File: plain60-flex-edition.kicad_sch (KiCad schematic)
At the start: 173 parts, among them J1 HRO-TYPE-C-31-M-12, J2 ISP, J3 ai03_ud, K1 KEYSW, K10 KEYSW, K11 KEYSW, K12 KEYSW, K13 KEYSW, K14 KEYSW, K15 KEYSW, K15-1 KEYSW, K16 KEYSW, K17 KEYSW, K18 KEYSW, K19 KEYSW, K2 KEYSW, K20 KEYSW, K21 KEYSW, K22 KEYSW, K23 KEYSW, K24 KEYSW, K25 KEYSW, K26 KEYSW, K27 KEYSW, K28 KEYSW, K29 KEYSW, K3 KEYSW, K31 KEYSW, K31-1 KEYSW, K32 KEYSW, K33 KEYSW, K34 KEYSW, K35 KEYSW, K36 KEYSW, K37 KEYSW, K38 KEYSW, K39 KEYSW, K4 KEYSW, K40 KEYSW, K41 KEYSW, K42 KEYSW, K43 KEYSW, K44 KEYSW, K44-1 KEYSW, K46 KEYSW, K46-1 KEYSW, K47 KEYSW, K48 KEYSW, K49 KEYSW, K5 KEYSW, K50 KEYSW, K51 KEYSW, K52 KEYSW, K53 KEYSW, K54 KEYSW, K55 KEYSW, K56 KEYSW, K57 KEYSW, K58 KEYSW, K58-1 KEYSW, K59 KEYSW, K6 KEYSW, K61 KEYSW, K61-1 KEYSW, K62 KEYSW, K62-1 KEYSW, K63 KEYSW, K63-1 KEYSW, K67 KEYSW, K67-1 KEYSW, K7 KEYSW, K71 KEYSW, K72 KEYSW, K72-1 KEYSW, K73 KEYSW, K73-1 KEYSW, K74 KEYSW, K74-1 KEYSW, K8 KEYSW, K9 KEYSW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

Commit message: added first iteration of refactoring
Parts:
- removed C1: 1u, Keeb_components:C_0805, symbol Device:C
- removed C2, C3, C4, C5: 0.1u, Keeb_components:C_0805, symbol Device:C
- removed C6: 4.7u, Keeb_components:C_0805, symbol Device:C
- removed F1: Polyfuse, Keeb_components:R_0805, symbol Device:Polyfuse
- removed H1: B0, footprints:free_pin, symbol Connector_Generic:Conn_01x01
- removed J1: HRO-TYPE-C-31-M-12, Keeb_components:HRO-TYPE-C-31-M-12, symbol Type-C:HRO-TYPE-C-31-M-12
- removed J2: ISP, Keeb_components:isp_standard, symbol Connector_Generic:Conn_02x03_Odd_Even
- removed J3: ai03_ud, Keeb_components:JST_SH_SM04B-SRSS-TB_1x04-1MP_P1.00mm_Horizontal, symbol Connector_Generic:Conn_01x04
- removed LS1: Speaker, Keeb_components:speaker_AST1109MLTRQ, symbol Device:Speaker
- removed R1, R2: 22, Keeb_components:R_0805, symbol Device:R
- removed R3, R4: 5.1k, Keeb_components:R_0805, symbol Device:R
- removed R5, R6: 10k, Keeb_components:R_0805, symbol Device:R
- removed SW1: SW_PUSH, Button_Switch_SMD:SW_SPST_TL3342, symbol keyboard_parts:SW_PUSH
- removed U1: ATmega32U4, Keeb_components:ATMEGA32U4, symbol atmel:ATmega32U4
- removed U2: USBLC6-2SC6, Keeb_components:USBLC6-2SC6, symbol keyboard_parts:USBLC6-2SC6
- removed X1: XTAL_GND, Keeb_components:Resonator_SMD_muRata_CSTNExxV-3Pin-p1.2, symbol keyboard_parts:XTAL_GND
- added J1: 4P4C, Connector_JST:JST_PH_S4B-PH-K_1x04_P2.00mm_Horizontal, symbol Connector:4P4C
- added U1: ProS3, footprints2:ProS3_TH, symbol ProS3:ProS3
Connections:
- net GND: now also J1.1, U1.2 (GND)
- net col0: now also U1.31 (IO34)
- net col1: now also U1.28 (IO7)
- net col10: now also U1.13 (IO16)
- net col11: now also U1.14 (IO15)
- net col12: now also U1.15 (IO14)
- net col13: now also U1.16 (IO13)
- net col14: now also U1.17 (IO12)
- net col2: now also U1.19 (IO41)
- net col3: now also U1.18 (IO42)
- net col4: now also U1.6 (IO2)
- net col5: now also U1.7 (IO3)
- net col6: now also U1.8 (IO4)
- net col7: now also U1.9 (IO5)
- net col8: now also U1.10 (IO21)
- net col9: now also U1.12 (LDO2_OUT)
- net row0: now also U1.34 (IO35)
- net row1: now also U1.33 (IO37)
- net row2: now also U1.32 (IO36)
- net row3: now also U1.22 (IO38)
- net row4: now also U1.21 (IO39)
- new net 5V: J1.2, U1.3 (5V)
- new net display SCL: J1.4, U1.30 (IO9)
- new net display SDA: J1.3, U1.29 (IO8)
- new net pin00 removed: U1.11 (IO0)
- new net pin03 unused: U1.27 (IO6)
- new net rgb R1: U1.20 (IO40)
- new net rx: U1.23 (RX)
- new net tx: U1.24 (TX)
- no-connect marks 12 -> 9
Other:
- moved on the sheet: D1, D10, D11, D12, D13, D14, D15, D16, D17, D18, D19, D2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

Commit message: tuning
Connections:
- net tx is gone; now on net pin00 removed: U1.24 (TX)
- net col0: now also U1.5 (IO1); no longer U1.31 (IO34)
- net pin00 removed: no longer U1.11 (IO0)
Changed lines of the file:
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@@
     )
   )
-  (global_label "col0" (shape input) (at 51.308 35.814 180)
-    (effects (font (size 0.9906 0.9906)) (justify right))
-    (property "Intersheet References" "${INTERSHEET_REFS}" (id 0) (at 245.618 96.774 0)
+  (global_label "col0" (shape input) (at 79.248 38.608 0)
+    (effects (font (size 0.9906 0.9906)) (justify left))
+    (property "Intersheet References" "${INTERSHEET_REFS}" (id 0) (at -115.062 -22.352 0)
       (effects (font (size 1.27 1.27)) hide)
     )
@@
     (property "Intersheet References" "${INTERSHEET_REFS}" (id 0) (at 16.764 -36.576 0)
       (effects (font (size 1.27 1.27)) hide)
-    )
-  )
-  (global_label "tx" (shape input) (at 51.308 53.848 180)
-    (effects (font (size 0.9906 0.9906)) (justify right))
-    (property "Intersheet References" "${INTERSHEET_REFS}" (id 0) (at 245.618 117.348 0)
-      (effects (font (size 0.9906 0.9906)) hide)
     )
   )
@@
     )
   )
-  (global_label "pin00 removed" (shape input) (at 79.248 53.848 0)
-    (effects (font (size 0.9906 0.9906)) (justify left))
-    (property "Intersheet References" "${INTERSHEET_REFS}" (id 0) (at -115.062 -7.112 0)
+  (global_label "pin00 removed" (shape input) (at 51.308 53.848 180)
+    (effects (font (size 0.9906 0.9906)) (justify right))
+    (property "Intersheet References" "${INTERSHEET_REFS}" (id 0) (at 245.618 114.808 0)
       (effects (font (size 0.9906 0.9906)) hide)
     )

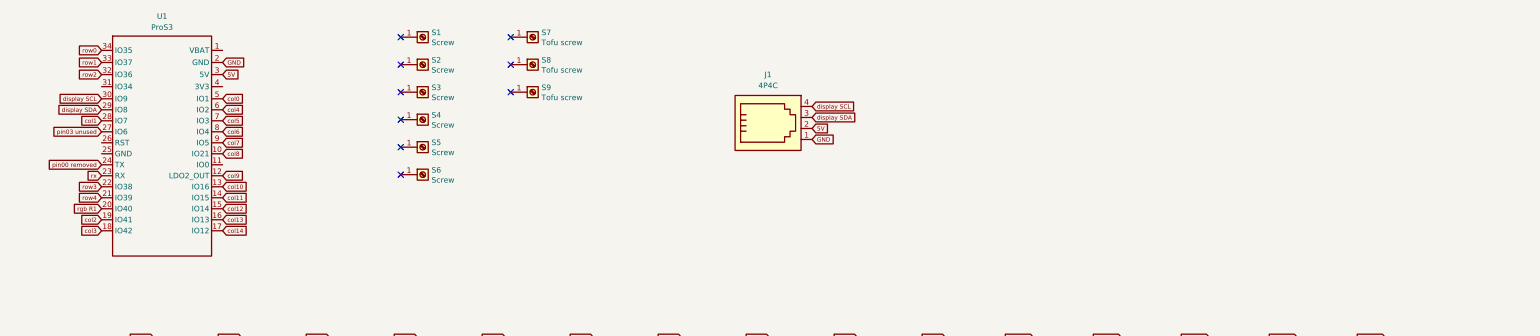
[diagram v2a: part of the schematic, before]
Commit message: added underglow leds
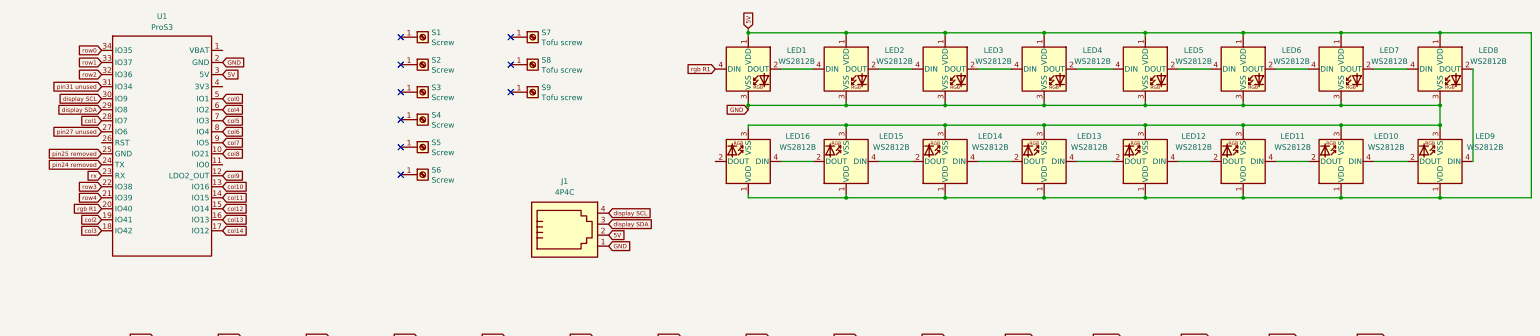
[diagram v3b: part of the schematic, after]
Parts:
- added LED1, LED10, LED11, LED12, LED13, LED14, LED15, LED16, LED2, LED3, LED4, LED5, LED6, LED7, LED8, LED9: WS2812B, LED_SMD:LED_WS2812B_PLCC4_5.0x5.0mm_P3.2mm, symbol LED:WS2812B
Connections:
- net 5V: now also LED1.1 (VDD), LED10.1 (VDD), LED11.1 (VDD), LED12.1 (VDD), LED13.1 (VDD), LED14.1 (VDD), LED15.1 (VDD), LED16.1 (VDD), LED2.1 (VDD), LED3.1 (VDD), LED4.1 (VDD), LED5.1 (VDD), LED6.1 (VDD), LED7.1 (VDD), LED8.1 (VDD), LED9.1 (VDD)
- net GND: now also LED1.3 (VSS), LED10.3 (VSS), LED11.3 (VSS), LED12.3 (VSS), LED13.3 (VSS), LED14.3 (VSS), LED15.3 (VSS), LED16.3 (VSS), LED2.3 (VSS), LED3.3 (VSS), LED4.3 (VSS), LED5.3 (VSS), LED6.3 (VSS), LED7.3 (VSS), LED8.3 (VSS), LED9.3 (VSS)
- net rgb R1: now also LED1.4 (DIN)
- net pin25 removed: now reaches U1.25 (GND)
- net pin31 unused: now reaches U1.31 (IO34)
- net pin00 removed renamed pin24 removed
- net pin03 unused renamed pin27 unused
- new net: LED15.2 (DOUT), LED16.4 (DIN)
- new net: LED14.2 (DOUT), LED15.4 (DIN)
- new net: LED13.2 (DOUT), LED14.4 (DIN)
- new net: LED12.2 (DOUT), LED13.4 (DIN)
- new net: LED6.2 (DOUT), LED7.4 (DIN)
- new net: LED5.2 (DOUT), LED6.4 (DIN)
- new net: LED10.2 (DOUT), LED11.4 (DIN)
- new net: LED10.4 (DIN), LED9.2 (DOUT)
- new net: LED11.2 (DOUT), LED12.4 (DIN)
- new net: LED4.2 (DOUT), LED5.4 (DIN)
- new net: LED7.2 (DOUT), LED8.4 (DIN)
- new net: LED3.2 (DOUT), LED4.4 (DIN)
- new net: LED2.2 (DOUT), LED3.4 (DIN)
- new net: LED8.2 (DOUT), LED9.4 (DIN)
- new net: LED1.2 (DOUT), LED2.4 (DIN)
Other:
- moved on the sheet: J1

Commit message: fix pins
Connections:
- net col9: now also U1.11 (IO0); no longer U1.12 (LDO2_OUT)
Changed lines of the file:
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@@
     )
   )
-  (global_label "col9" (shape input) (at 79.248 56.388 0)
+  (global_label "col9" (shape input) (at 79.248 53.848 0)
     (effects (font (size 0.9906 0.9906)) (justify left))
-    (property "Intersheet References" "${INTERSHEET_REFS}" (id 0) (at -115.062 5.588 0)
+    (property "Intersheet References" "${INTERSHEET_REFS}" (id 0) (at -115.062 3.048 0)
       (effects (font (size 1.27 1.27)) hide)
     )

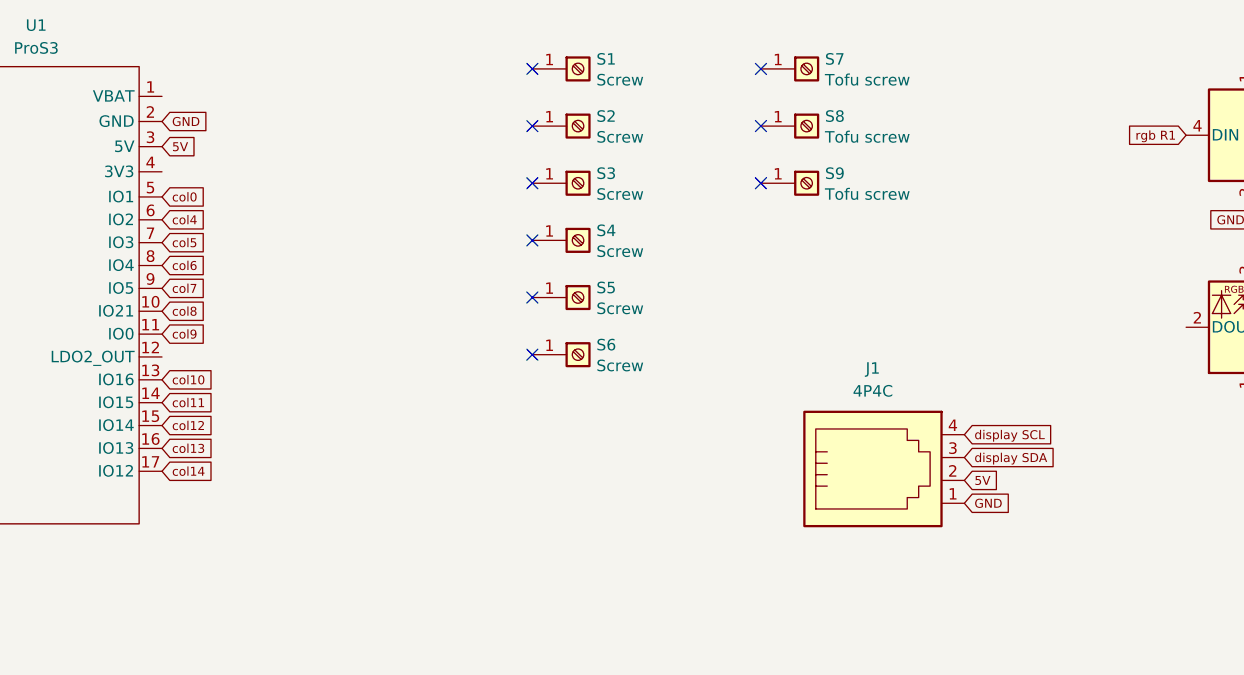
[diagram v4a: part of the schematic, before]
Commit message: fixed JST header direction
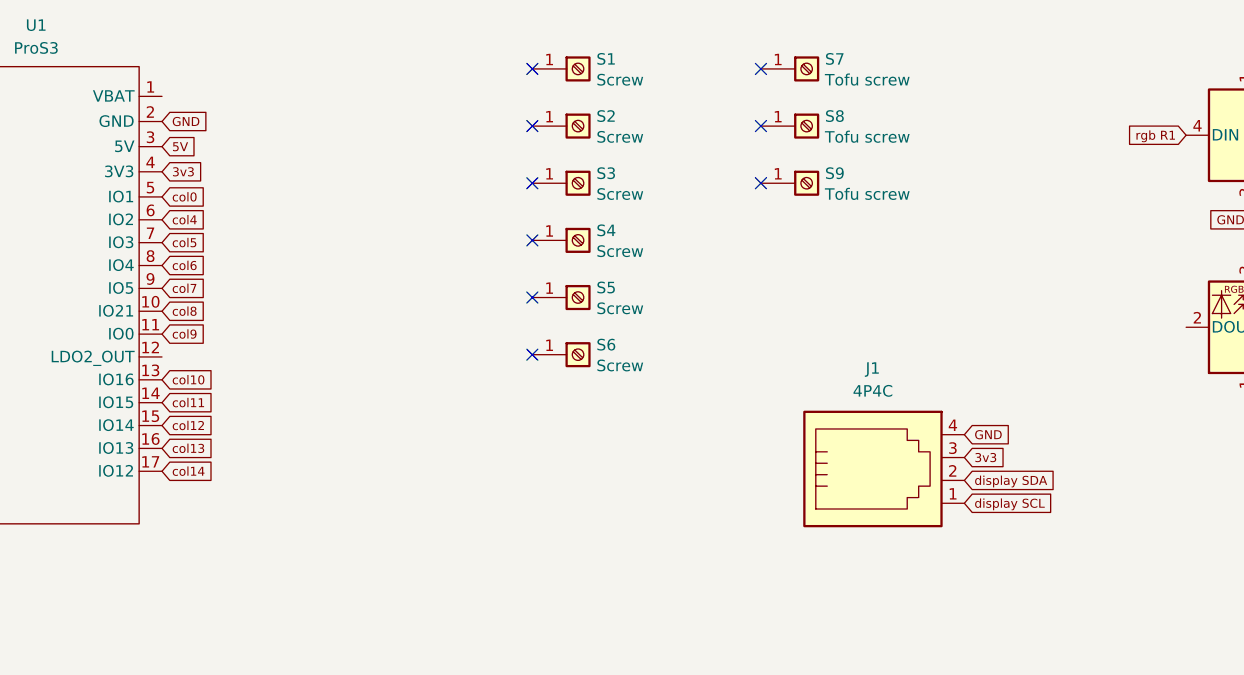
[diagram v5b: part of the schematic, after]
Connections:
- net 5V: no longer J1.2
- net GND: now also J1.4; no longer J1.1
- net display SCL: now also J1.1; no longer J1.4
- net display SDA: now also J1.2; no longer J1.3
- net 3v3: now reaches U1.4 (3V3)
- net 3v3: now also J1.3
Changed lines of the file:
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@@
+    )
+  )
+  (global_label "3v3" (shape input) (at 79.248 35.814 0) (fields_autoplaced)
+    (effects (font (size 0.9906 0.9906)) (justify left))
+    (property "Intersheet References" "${INTERSHEET_REFS}" (id 0) (at 83.7717 35.7521 0)
+      (effects (font (size 0.9906 0.9906)) (justify left) hide)
     )
   )
@@
     )
   )
-  (global_label "display SDA" (shape input) (at 168.402 67.564 0) (fields_autoplaced)
+  (global_label "display SDA" (shape input) (at 168.402 70.104 0) (fields_autoplaced)
     (effects (font (size 0.9906 0.9906)) (justify left))
-    (property "Intersheet References" "${INTERSHEET_REFS}" (id 0) (at 179.058 67.6259 0)
+    (property "Intersheet References" "${INTERSHEET_REFS}" (id 0) (at 179.058 70.1659 0)
       (effects (font (size 0.9906 0.9906)) (justify left) hide)
     )
@@
     )
   )
-  (global_label "GND" (shape input) (at 168.402 72.644 0) (fields_autoplaced)
+  (global_label "GND" (shape input) (at 168.402 65.024 0) (fields_autoplaced)
     (effects (font (size 0.9906 0.9906)) (justify left))
-    (property "Intersheet References" "${INTERSHEET_REFS}" (id 0) (at 173.3031 72.5821 0)
+    (property "Intersheet References" "${INTERSHEET_REFS}" (id 0) (at 173.3031 64.9621 0)
       (effects (font (size 0.9906 0.9906)) (justify left) hide)
     )
@@
     )
   )
-  (global_label "display SCL" (shape input) (at 168.402 65.024 0) (fields_autoplaced)
+  (global_label "display SCL" (shape input) (at 168.402 72.644 0) (fields_autoplaced)
     (effects (font (size 0.9906 0.9906)) (justify left))
-    (property "Intersheet References" "${INTERSHEET_REFS}" (id 0) (at 179.0108 65.0859 0)
+    (property "Intersheet References" "${INTERSHEET_REFS}" (id 0) (at 179.0108 72.7059 0)
       (effects (font (size 0.9906 0.9906)) (justify left) hide)
     )
@@
     )
   )
-  (global_label "5V" (shape input) (at 168.402 70.104 0) (fields_autoplaced)
+  (global_label "3v3" (shape input) (at 168.402 67.564 0) (fields_autoplaced)
     (effects (font (size 0.9906 0.9906)) (justify left))
-    (property "Intersheet References" "${INTERSHEET_REFS}" (id 0) (at 172.0766 70.0421 0)
+    (property "Intersheet References" "${INTERSHEET_REFS}" (id 0) (at 172.9257 67.5021 0)
       (effects (font (size 0.9906 0.9906)) (justify left) hide)
     )
